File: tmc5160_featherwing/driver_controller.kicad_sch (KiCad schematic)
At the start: 2 parts, among them J2 Conn_01x04_P3.5MM_TBH_Horizon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, U1 TMC5160A-WA

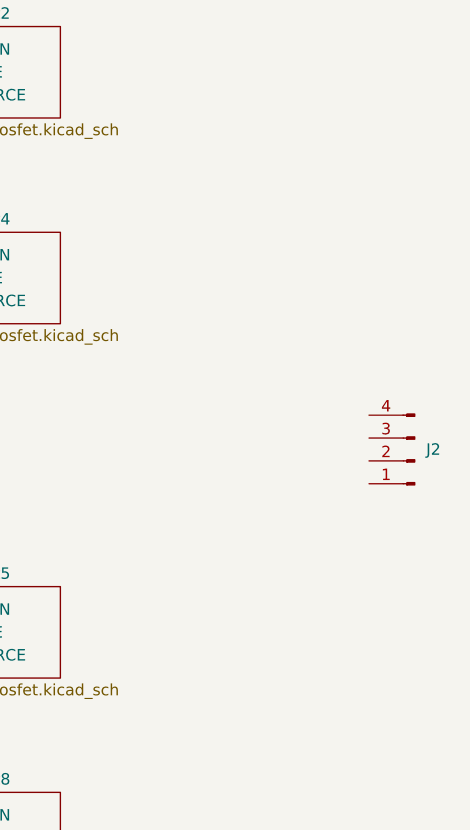
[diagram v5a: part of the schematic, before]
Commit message: Adjust connectors
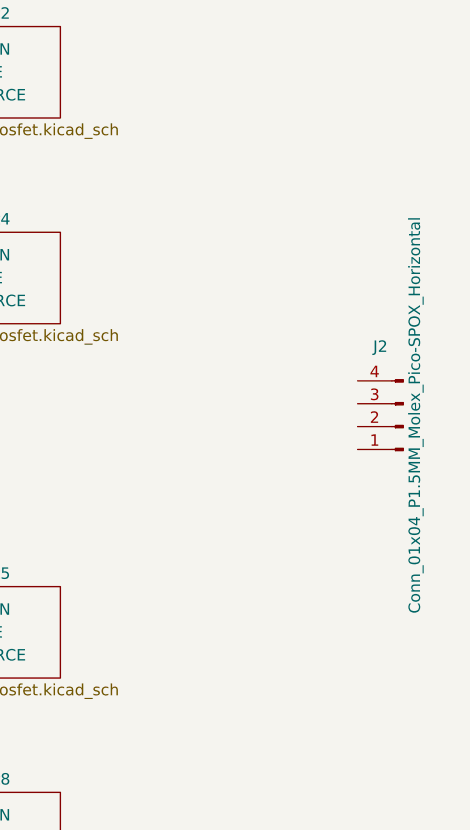
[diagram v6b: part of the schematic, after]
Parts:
- removed J2: Conn_01x04_P3.5MM_TBH_Horizontal_Screw, Janelia:PhoenixContact_MC_1,5_4-G-3.5_1x04_P3.50mm_Horizontal_Push, symbol Janelia:Conn_01x04_P3.5MM_TBH_Horizontal_Push
- added J2: Conn_01x04_P1.5MM_Molex_Pico-SPOX_Horizontal, Janelia:Molex_Pico-SPOX_87438_1x04-P1.5mm_Horizontal, symbol Janelia:Conn_01x04_P1.5MM_Molex_Pico-SPOX_Horizontal
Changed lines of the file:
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@@
   (title_block
     (title "tmc5160_featherwing")
-    (date "2024-03-25")
+    (date "2024-04-04")
     (rev "1.0")
     (company "Howard Hughes Medical Institute")
-  )
-  (symbol (lib_id "Janelia:Conn_01x04_P3.5MM_TBH_Horizontal_Push") (at 246.38 87.63 180) (unit 1)
-    (in_bom yes) (on_board yes) (dnp no) (fields_autoplaced)
-    (property "Reference" "J2" (at 247.65 86.36 0)
-      (effects (font (size 1.27 1.27)) (justify right))
-    )
-    (property "Value" "Conn_01x04_P3.5MM_TBH_Horizontal_Screw" (at 246.38 74.93 0)
-      (effects (font (size 1.27 1.27)) hide)
-    )
-    (property "Footprint" "Janelia:PhoenixContact_MC_1,5_4-G-3.5_1x04_P3.50mm_Horizontal_Push" (at 246.38 123.19 0)
-      (effects (font (size 1.27 1.27)) hide)
-    )
-    (property "Datasheet" "" (at 246.38 107.95 0)
-      (effects (font (size 1.27 1.27)) hide)
-    )
-    (property "Manufacturer" "Phoenix Contact" (at 246.38 120.65 0)
-      (effects (font (size 1.27 1.27)) hide)
-    )
-    (property "Manufacturer Part Number" "1844236" (at 246.38 115.57 0)
-      (effects (font (size 1.27 1.27)) hide)
-    )
-    (property "Description" "TERM BLOCK HDR 4POS 90DEG 3.5MM" (at 246.38 113.03 0)
-      (effects (font (size 1.27 1.27)) hide)
-    )
-    (property "Vendor" "Digi-Key" (at 246.38 118.11 0)
-      (effects (font (size 1.27 1.27)) hide)
-    )
-    (property "Vendor Part Number" "277-2419-ND" (at 246.38 110.49 0)
-      (effects (font (size 1.27 1.27)) hide)
-    )
-    (property "Sim.Enable" "0" (at 246.38 87.63 0)
-      (effects (font (size 1.27 1.27)) hide)
-    )
-    (pin "4")
-    (pin "2")
-    (pin "3")
-    (pin "1")
-    (instances
-      (project "tmc5160_featherwing"
-        (path "/df2b2e89-e055-4140-95de-f1df723db034/039ac378-5273-4081-85bf-9eb26cb5ed57"
-          (reference "J2") (unit 1)
-        )
-      )
-    )
   )
   (symbol (lib_id "Janelia:TMC5160A-WA") (at 62.23 88.9 0) (unit 1)
@@
         )
       )
+    )
+  )
+  (symbol (lib_id "Janelia:Conn_01x04_P1.5MM_Molex_Pico-SPOX_Horizontal") (at 245.11 83.82 180) (unit 1)
+    (in_bom yes) (on_board yes) (dnp no)
+    (property "Reference" "J2" (at 242.57 74.93 0) (do_not_autoplace)
+      (effects (font (size 1.27 1.27)))
+    )
+    (property "Value" "Conn_01x04_P1.5MM_Molex_Pico-SPOX_Horizontal" (at 246.38 82.55 90) (do_not_autoplace)
+      (effects (font (size 1.27 1.27)))
+    )
+    (property "Footprint" "Janelia:Molex_Pico-SPOX_87438_1x04-P1.5mm_Horizontal" (at 245.11 83.82 0)
+      (effects (font (size 1.27 1.27)) hide)
+    )
+    (property "Datasheet" "~" (at 245.11 83.82 0)
+      (effects (font (size 1.27 1.27)) hide)
+    )
+    (property "Description" "CONN HEADER SMD R/A 4POS 1.5MM" (at 245.11 83.82 0)
+      (effects (font (size 1.27 1.27)) hide)
+    )
+    (property "Manufacturer" "Molex" (at 245.11 83.82 0)
+      (effects (font (size 1.27 1.27)) hide)
+    )
+    (property "Manufacturer Part Number" "0874380443" (at 245.11 83.82 0)
+      (effects (font (size 1.27 1.27)) hide)
+    )
+    (property "Vendor" "Digi-Key" (at 245.11 83.82 0)
+      (effects (font (size 1.27 1.27)) hide)
+    )
+    (property "Vendor Part Number" "WM7648CT-ND" (at 245.11 83.82 0)
+      (effects (font (size 1.27 1.27)) hide)
+    )
+    (pin "4")
+    (pin "3")
+    (pin "2")
+    (pin "1")
+    (instances
+      (project "tmc5160_featherwing"
+        (path "/df2b2e89-e055-4140-95de-f1df723db034/039ac378-5273-4081-85bf-9eb26cb5ed57"
+          (reference "J2") (unit 1)
+        )
+      )

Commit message: Add to power sheet
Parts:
- removed J2: Conn_01x04_P1.5MM_Molex_Pico-SPOX_Horizontal, Janelia:Molex_Pico-SPOX_87438_1x04-P1.5mm_Horizontal, symbol Janelia:Conn_01x04_P1.5MM_Molex_Pico-SPOX_Horizontal
- added J4: Conn_01x04_P1.5MM_Molex_Pico-SPOX-87438_Horizontal, Janelia:Molex_Pico-SPOX-87438_1x04-P1.5mm_Horizontal, symbol Janelia:Conn_01x04_P1.5MM_Molex_Pico-SPOX-87438_Horizontal
- added J5: Conn_01x02_P1.5MM_Molex_Pico-SPOX_Horizontal, Janelia:Molex_Pico-Clasp-501568_1x02_P1MM_Horizontal, symbol Janelia:Conn_01x02_P1MM_Molex_Pico-Clasp-501330_Horizontal
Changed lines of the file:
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@@
   (title_block
     (title "tmc5160_featherwing")
-    (date "2024-04-04")
+    (date "2024-04-05")
     (rev "1.0")
     (company "Howard Hughes Medical Institute")
+  )
+  (symbol (lib_id "Janelia:Conn_01x04_P1.5MM_Molex_Pico-SPOX-87438_Horizontal") (at 245.11 83.82 180) (unit 1)
+    (in_bom yes) (on_board yes) (dnp no)
+    (property "Reference" "J4" (at 242.57 74.93 0) (do_not_autoplace)
+      (effects (font (size 1.27 1.27)))
+    )
+    (property "Value" "Conn_01x04_P1.5MM_Molex_Pico-SPOX-87438_Horizontal" (at 246.38 82.55 90) (do_not_autoplace)
+      (effects (font (size 1.27 1.27)) hide)
+    )
+    (property "Footprint" "Janelia:Molex_Pico-SPOX-87438_1x04-P1.5mm_Horizontal" (at 245.11 83.82 0)
+      (effects (font (size 1.27 1.27)) hide)
+    )
+    (property "Datasheet" "~" (at 245.11 83.82 0)
+      (effects (font (size 1.27 1.27)) hide)
+    )
+    (property "Description" "CONN HEADER SMD R/A 4POS 1.5MM" (at 245.11 83.82 0)
+      (effects (font (size 1.27 1.27)) hide)
+    )
+    (property "Manufacturer" "Molex" (at 245.11 83.82 0)
+      (effects (font (size 1.27 1.27)) hide)
+    )
+    (property "Manufacturer Part Number" "0874380443" (at 245.11 83.82 0)
+      (effects (font (size 1.27 1.27)) hide)
+    )
+    (property "Vendor" "Digi-Key" (at 245.11 83.82 0)
+      (effects (font (size 1.27 1.27)) hide)
+    )
+    (property "Vendor Part Number" "WM7648CT-ND" (at 245.11 83.82 0)
+      (effects (font (size 1.27 1.27)) hide)
+    )
+    (pin "1")
+    (pin "2")
+    (pin "4")
+    (pin "3")
+    (instances
+      (project "tmc5160_featherwing"
+        (path "/df2b2e89-e055-4140-95de-f1df723db034/039ac378-5273-4081-85bf-9eb26cb5ed57"
+          (reference "J4") (unit 1)
+        )
+      )
+    )
   )
   (symbol (lib_id "Janelia:TMC5160A-WA") (at 62.23 88.9 0) (unit 1)
@@
     )
   )
-  (symbol (lib_id "Janelia:Conn_01x04_P1.5MM_Molex_Pico-SPOX_Horizontal") (at 245.11 83.82 180) (unit 1)
+  (symbol (lib_id "Janelia:Conn_01x02_P1MM_Molex_Pico-Clasp-501330_Horizontal") (at 245.11 138.43 180) (unit 1)
     (in_bom yes) (on_board yes) (dnp no)
-    (property "Reference" "J2" (at 242.57 74.93 0) (do_not_autoplace)
+    (property "Reference" "J5" (at 242.57 132.08 0) (do_not_autoplace)
       (effects (font (size 1.27 1.27)))
     )
-    (property "Value" "Conn_01x04_P1.5MM_Molex_Pico-SPOX_Horizontal" (at 246.38 82.55 90) (do_not_autoplace)
-      (effects (font (size 1.27 1.27)))
-    )
-    (property "Footprint" "Janelia:Molex_Pico-SPOX_87438_1x04-P1.5mm_Horizontal" (at 245.11 83.82 0)
+    (property "Value" "Conn_01x02_P1.5MM_Molex_Pico-SPOX_Horizontal" (at 246.38 137.16 90) (do_not_autoplace)
       (effects (font (size 1.27 1.27)) hide)
     )
-    (property "Datasheet" "~" (at 245.11 83.82 0)
+    (property "Footprint" "Janelia:Molex_Pico-Clasp-501568_1x02_P1MM_Horizontal" (at 245.11 138.43 0)
       (effects (font (size 1.27 1.27)) hide)
     )
-    (property "Description" "CONN HEADER SMD R/A 4POS 1.5MM" (at 245.11 83.82 0)
+    (property "Datasheet" "~" (at 245.11 138.43 0)
       (effects (font (size 1.27 1.27)) hide)
     )
-    (property "Manufacturer" "Molex" (at 245.11 83.82 0)
+    (property "Description" "CONN HEADER SMD R/A 2POS 1MM" (at 245.11 138.43 0)
       (effects (font (size 1.27 1.27)) hide)
     )
-    (property "Manufacturer Part Number" "0874380443" (at 245.11 83.82 0)
+    (property "Manufacturer" "Molex" (at 245.11 138.43 0)
       (effects (font (size 1.27 1.27)) hide)
     )
-    (property "Vendor" "Digi-Key" (at 245.11 83.82 0)
+    (property "Manufactuer Part Number" "5015680207" (at 245.11 138.43 0)
       (effects (font (size 1.27 1.27)) hide)
     )
-    (property "Vendor Part Number" "WM7648CT-ND" (at 245.11 83.82 0)
+    (property "Vendor" "Digi-Key" (at 245.11 138.43 0)
       (effects (font (size 1.27 1.27)) hide)
     )
-    (pin "4")
-    (pin "3")
+    (property "Vendor Part Number" "WM7893CT-ND" (at 245.11 138.43 0)
+      (effects (font (size 1.27 1.27)) hide)
+    )
+    (pin "1")
     (pin "2")
-    (pin "1")
     (instances
       (project "tmc5160_featherwing"
         (path "/df2b2e89-e055-4140-95de-f1df723db034/039ac378-5273-4081-85bf-9eb26cb5ed57"
-          (reference "J2") (unit 1)
+          (reference "J5") (unit 1)
         )
       )

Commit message: Add parts
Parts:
- added U11: MAX6816, Janelia:SOT192P237X122-4N, symbol Janelia:MAX6816
- added X1: 16MHz, Janelia:OSC_ECS-2520S33-160-FN-TR, symbol Janelia:Oscillator_16MHz_ECS-2520S33
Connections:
- net GND: now reaches U1.12 (TST_MODE)
- net GND: now also U1.19 (REFR/DIR), U1.21 (SD_MODE), U1.25 (GNDD), U1.26 (ENCN/DCO/CFG6), U1.29 (~{DRV_EN}), U1.48 (EP), U1.7 (GNDA), X1.2 (GND)
- net CLOCK: now reaches U1.13 (CLK)
- net CLOCK: now also X1.3 (OUT)
- net ~{CS}: now reaches U1.14 (~{CS}/CFG3)
- net SCK: now reaches U1.15 (SCK/CFG2)
- net MOSI: now reaches U1.16 (SDI/CFG1)
- net MISO: now reaches U1.17 (SDO/CFG0)
- net VIO: now reaches U1.22 (SPI_MODE)
- net VIO: now also X1.4 (VDD)
- no-connect marks 0 -> 5
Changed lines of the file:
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@@
   (title_block
     (title "tmc5160_featherwing")
-    (date "2024-04-05")
+    (date "2024-04-10")
     (rev "1.0")
     (company "Howard Hughes Medical Institute")
+  )
+  (no_connect (at 44.45 93.98))
+  (no_connect (at 19.05 154.94))
+  (no_connect (at 44.45 104.14))
+  (no_connect (at 44.45 106.68))
+  (no_connect (at 44.45 91.44))
+  (wire (pts (xy 62.23 127) (xy 62.23 129.54))
+    (stroke (width 0) (type default))
+  )
+  (wire (pts (xy 29.21 35.56) (xy 31.75 35.56))
+    (stroke (width 0) (type default))
+  )
+  (wire (pts (xy 44.45 88.9) (xy 41.91 88.9))
+    (stroke (width 0) (type default))
+  )
+  (wire (pts (xy 59.69 127) (xy 59.69 129.54))
+    (stroke (width 0) (type default))
+  )
+  (wire (pts (xy 44.45 63.5) (xy 41.91 63.5))
+    (stroke (width 0) (type default))
+  )
+  (wire (pts (xy 44.45 121.92) (xy 41.91 121.92))
+    (stroke (width 0) (type default))
+  )
+  (wire (pts (xy 29.21 147.32) (xy 29.21 144.78))
+    (stroke (width 0) (type default))
+  )
+  (wire (pts (xy 44.45 83.82) (xy 41.91 83.82))
+    (stroke (width 0) (type default))
+  )
+  (wire (pts (xy 44.45 116.84) (xy 41.91 116.84))
+    (stroke (width 0) (type default))
+  )
+  (wire (pts (xy 39.37 154.94) (xy 41.91 154.94))
+    (stroke (width 0) (type default))
+  )
+  (wire (pts (xy 29.21 162.56) (xy 29.21 165.1))
+    (stroke (width 0) (type default))
+  )
+  (wire (pts (xy 44.45 99.06) (xy 41.91 99.06))
+    (stroke (width 0) (type default))
+  )
+  (wire (pts (xy 64.77 127) (xy 64.77 129.54))
+    (stroke (width 0) (type default))
+  )
+  (wire (pts (xy 44.45 73.66) (xy 41.91 73.66))
+    (stroke (width 0) (type default))
+  )
+  (wire (pts (xy 29.21 30.48) (xy 31.75 30.48))
+    (stroke (width 0) (type default))
+  )
+  (wire (pts (xy 44.45 71.12) (xy 41.91 71.12))
+    (stroke (width 0) (type default))
+  )
+  (wire (pts (xy 44.45 68.58) (xy 41.91 68.58))
+    (stroke (width 0) (type default))
+  )
+  (wire (pts (xy 44.45 119.38) (xy 41.91 119.38))
+    (stroke (width 0) (type default))
+  )
+  (wire (pts (xy 44.45 76.2) (xy 41.91 76.2))
+    (stroke (width 0) (type default))
+  )
+  (wire (pts (xy 29.21 33.02) (xy 31.75 33.02))
+    (stroke (width 0) (type default))
+  )
+  (label "VIO" (at 29.21 144.78 90) (fields_autoplaced)
+    (effects (font (size 1.27 1.27)) (justify left bottom))
+  )
+  (label "SCK" (at 41.91 71.12 180) (fields_autoplaced)
+    (effects (font (size 1.27 1.27)) (justify right bottom))
+  )
+  (label "GND" (at 41.91 83.82 180) (fields_autoplaced)
+    (effects (font (size 1.27 1.27)) (justify right bottom))
+  )
+  (label "GND" (at 41.91 116.84 180) (fields_autoplaced)
+    (effects (font (size 1.27 1.27)) (justify right bottom))
+  )
+  (label "VIO" (at 31.75 33.02 0) (fields_autoplaced)
+    (effects (font (size 1.27 1.27)) (justify left bottom))
+  )
+  (label "GND" (at 41.91 121.92 180) (fields_autoplaced)
+    (effects (font (size 1.27 1.27)) (justify right bottom))
+  )
+  (label "MOSI" (at 41.91 73.66 180) (fields_autoplaced)
+    (effects (font (size 1.27 1.27)) (justify right bottom))
+  )
+  (label "GND" (at 41.91 99.06 180) (fields_autoplaced)
+    (effects (font (size 1.27 1.27)) (justify right bottom))
+  )
+  (label "MISO" (at 41.91 76.2 180) (fields_autoplaced)
+    (effects (font (size 1.27 1.27)) (justify right bottom))
+  )
+  (label "~{CS}" (at 41.91 68.58 180) (fields_autoplaced)
+    (effects (font (size 1.27 1.27)) (justify right bottom))
+  )
+  (label "GND" (at 41.91 88.9 180) (fields_autoplaced)
+    (effects (font (size 1.27 1.27)) (justify right bottom))
+  )
+  (label "VM" (at 31.75 30.48 0) (fields_autoplaced)
+    (effects (font (size 1.27 1.27)) (justify left bottom))
+  )
+  (label "GND" (at 62.23 129.54 270) (fields_autoplaced)
+    (effects (font (size 1.27 1.27)) (justify right bottom))
+  )
+  (label "GND" (at 29.21 165.1 270) (fields_autoplaced)
+    (effects (font (size 1.27 1.27)) (justify right bottom))
+  )
+  (label "VIO" (at 41.91 119.38 180) (fields_autoplaced)
+    (effects (font (size 1.27 1.27)) (justify right bottom))
+  )
+  (label "GND" (at 64.77 129.54 270) (fields_autoplaced)
+    (effects (font (size 1.27 1.27)) (justify right bottom))
+  )
+  (label "GND" (at 31.75 35.56 0) (fields_autoplaced)
+    (effects (font (size 1.27 1.27)) (justify left bottom))
+  )
+  (label "CLOCK" (at 41.91 63.5 180) (fields_autoplaced)
+    (effects (font (size 1.27 1.27)) (justify right bottom))
+  )
+  (label "CLOCK" (at 41.91 154.94 0) (fields_autoplaced)
+    (effects (font (size 1.27 1.27)) (justify left bottom))
+  )
+  (label "GND" (at 59.69 129.54 270) (fields_autoplaced)
+    (effects (font (size 1.27 1.27)) (justify right bottom))
+  )
+  (hierarchical_label "VIO" (shape passive) (at 29.21 33.02 180) (fields_autoplaced)
+    (effects (font (size 1.27 1.27)) (justify right))
+  )
+  (hierarchical_label "VM" (shape passive) (at 29.21 30.48 180) (fields_autoplaced)
+    (effects (font (size 1.27 1.27)) (justify right))
+  )
+  (hierarchical_label "GND" (shape passive) (at 29.21 35.56 180) (fields_autoplaced)
+    (effects (font (size 1.27 1.27)) (justify right))
   )
   (symbol (lib_id "Janelia:Conn_01x04_P1.5MM_Molex_Pico-SPOX-87438_Horizontal") (at 245.11 83.82 180) (unit 1)
@@
         (path "/df2b2e89-e055-4140-95de-f1df723db034/039ac378-5273-4081-85bf-9eb26cb5ed57"
           (reference "J4") (unit 1)
+        )
+      )
+    )
+  )
+  (symbol (lib_id "Janelia:MAX6816") (at 229.87 151.13 0) (unit 1)
+    (in_bom yes) (on_board yes) (dnp no)
+    (property "Reference" "U11" (at 236.22 144.78 0)
+      (effects (font (size 1.524 1.524)))
+    )
+    (property "Value" "MAX6816" (at 236.22 157.48 0)
+      (effects (font (size 1.524 1.524)))
+    )
+    (property "Footprint" "Janelia:SOT192P237X122-4N" (at 229.87 170.18 0)
+      (effects (font (size 1.524 1.524)) hide)
+    )
+    (property "Datasheet" "" (at 229.87 151.13 0)
+      (effects (font (size 1.524 1.524)))
+    )
+    (property "Description" "IC SWITCH DEBOUNCER" (at 229.87 167.64 0)
+      (effects (font (size 1.524 1.524)) hide)
+    )
+    (property "Package" " SOT143-4" (at 229.87 151.13 0)
+      (effects (font (size 1.524 1.524)) hide)
+    )
+    (property "Manufacturer" "Analog Devices Inc./Maxim Integrated" (at 229.87 151.13 0)
+      (effects (font (size 1.524 1.524)) hide)
+    )
+    (property "Manufacturer Part Number" "MAX6816EUS+T" (at 229.87 151.13 0)
+      (effects (font (size 1.524 1.524)) hide)
+    )
+    (property "Vendor" "Digi-Key" (at 229.87 175.26 0)
+      (effects (font (size 1.524 1.524)) hide)
+    )
+    (property "Vendor Part Number" "MAX6816EUS+TCT-ND" (at 229.87 172.72 0)
+      (effects (font (size 1.524 1.524)) hide)
+    )
+    (property "Sim.Enable" "0" (at 229.87 151.13 0)
+      (effects (font (size 1.27 1.27)) hide)
+    )
+    (pin "1")
+    (pin "3")
+    (pin "4")
+    (pin "2")
+    (instances
+      (project "tmc5160_featherwing"
+        (path "/df2b2e89-e055-4140-95de-f1df723db034/039ac378-5273-4081-85bf-9eb26cb5ed57"
+          (reference "U11") (unit 1)
         )
       )
@@
         )
       )
+    )
+  )
+  (symbol (lib_id "Janelia:Oscillator_16MHz_ECS-2520S33") (at 29.21 154.94 0) (unit 1)
+    (in_bom yes) (on_board yes) (dnp no)
+    (property "Reference" "X1" (at 34.29 148.59 0)
+      (effects (font (size 1.27 1.27)))
+    )
+    (property "Value" "16MHz" (at 34.29 161.29 0)
+      (effects (font (size 1.27 1.27)))
+    )
+    (property "Footprint" "Janelia:OSC_ECS-2520S33-160-FN-TR" (at 40.64 163.83 0)
+      (effects (font (size 1.27 1.27)) hide)
+    )
+    (property "Datasheet" "" (at 24.765 151.765 0)
+      (effects (font (size 1.27 1.27)) hide)
+    )
+    (property "Description" "XTAL OSC XO 16.0000MHZ HCMOS SMD" (at 29.21 154.94 0)
+      (effects (font (size 1.27 1.27)) hide)
+    )
+    (property "Manufacturer" "ECS Inc." (at 29.21 154.94 0)
+      (effects (font (size 1.27 1.27)) hide)
+    )
+    (property "Manufacturer Part Number" "ECS-2520S33-160-FN-TR" (at 29.21 154.94 0)
+      (effects (font (size 1.27 1.27)) hide)
+    )
+    (property "Vendor" "Digi-Key" (at 29.21 154.94 0)
+      (effects (font (size 1.27 1.27)) hide)
+    )
+    (property "Vendor Part Number" "XC2195CT-ND" (at 29.21 154.94 0)
+      (effects (font (size 1.27 1.27)) hide)
+    )
+    (pin "4")
+    (pin "3")
+    (pin "1")
+    (pin "2")
+    (instances
+      (project "tmc5160_featherwing"
+        (path "/df2b2e89-e055-4140-95de-f1df723db034/039ac378-5273-4081-85bf-9eb26cb5ed57"
+          (reference "X1") (unit 1)
+        )
+      )
